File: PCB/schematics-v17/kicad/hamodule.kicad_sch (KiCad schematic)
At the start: 83 parts, among them J1 2604-1104, J10 EspSense, J11 Conn_01x02_Male, J12 NoCon, J2 2604-1102, J3 USB_C_Receptacle_USB2.0, J4 ESP Relays, J5 Current Jumper, J6 GND 3.3V, J7 Conn_01x02, J8 Current Jumper, J9 2604-1104, K1 PCN-105D, K2 PCN-105D, K3 PCN-105D, K4 PCN-105D, Q1 SS8050, Q2 SS8050, SW1 EN, SW2 IO0, U1 ULN2003A, U2 ESP32-WROOM-32E, U4 LD1117AV33_TO220, U5 MCP9700T-ETT, U6 LDA210-PDIP, U7 LDA210-PDIP, U8 CP2102N-A01-GQFN28

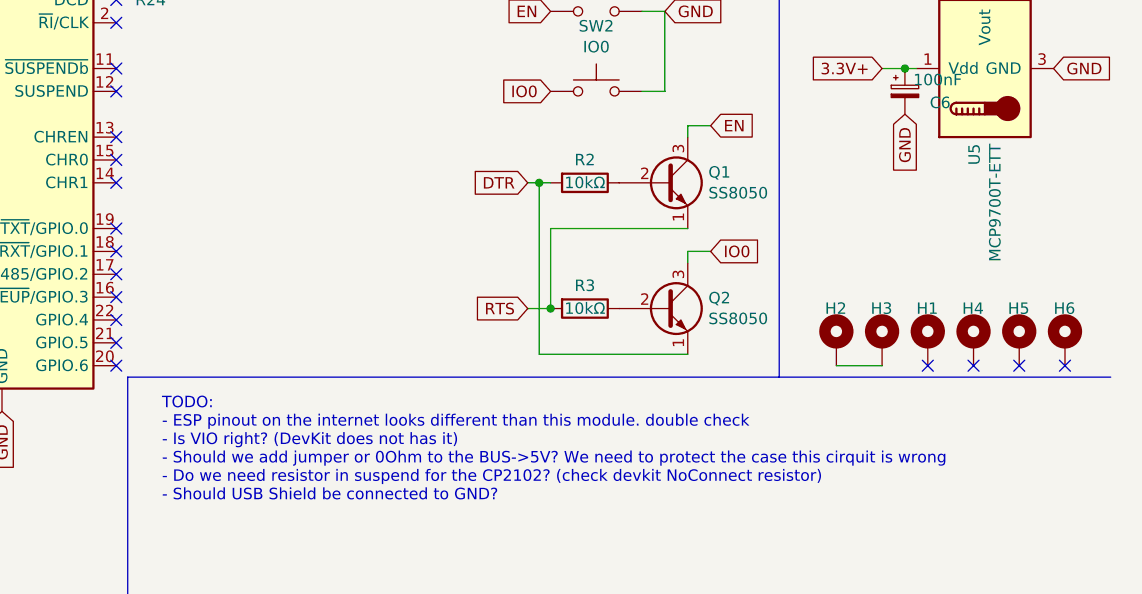
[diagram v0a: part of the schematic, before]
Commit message: fixing transistor symbol. pinout was wrong :(
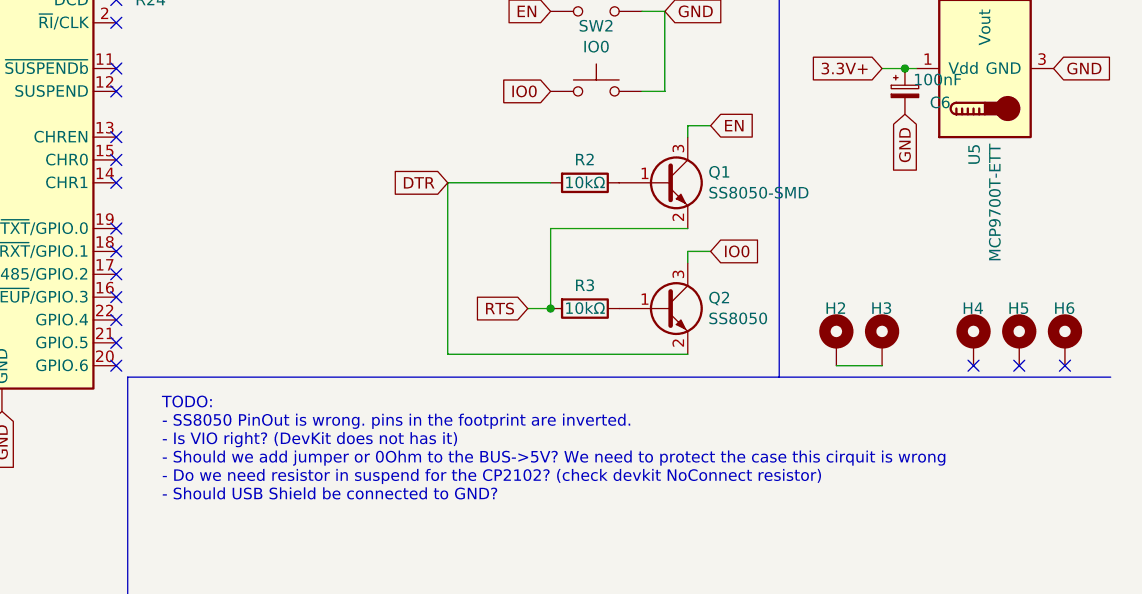
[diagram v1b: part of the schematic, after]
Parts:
- removed H1: MountingHole_Pad, MountingHole:MountingHole_3.2mm_M3_ISO14580_Pad, symbol Mechanical:MountingHole_Pad
- Q1: value SS8050 -> SS8050-SMD
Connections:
- net DTR: now also Q2.2 (E); no longer Q2.1 (E)
- net RTS: now also Q1.2 (E); no longer Q1.1 (E)
- net at R2.1: now also Q1.1 (B); no longer Q1.2 (B)
- net at R3.1: now also Q2.1 (B); no longer Q2.2 (B)
- no-connect marks 52 -> 51
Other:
- note added: "TODO: - SS8050 PinOut is wrong. pins in the footprint are inverted. - Is VIO right? (DevKit does not has it) - Should we add jumper or 0Ohm to the BUS->5V? We need to protect the case this cirquit is wrong - Do we need resistor in suspend for the CP2102? (check devkit NoConnect resistor) - Should USB Shield be connected to GND?"
- note removed: "TODO: - ESP pinout on the internet looks different than this module. double check - Is VIO right? (DevKit does not has it) - Should we add jumper or 0Ohm to the BUS->5V? We need to protect the case this cirquit is wrong - Do we need resistor in suspend for the CP2102? (check devkit NoConnect resistor) - Should USB Shield be connected to GND?"
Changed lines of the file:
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@@
   (junction (at 114.3 86.36) (diameter 0) (color 0 0 0 0)
   )
-  (junction (at 220.98 143.51) (diameter 0) (color 0 0 0 0)
-  )
   (junction (at 135.89 60.96) (diameter 0) (color 0 0 0 0)
   )
@@
   (no_connect (at 67.31 146.05))
   (no_connect (at 57.15 39.37))
-  (no_connect (at 264.16 163.83))
   (no_connect (at 173.99 148.59))
   (no_connect (at 173.99 161.29))
@@
     (stroke (width 0) (type default) (color 0 0 0 0))
   )
-  (wire (pts (xy 220.98 143.51) (xy 220.98 162.56))
-    (stroke (width 0) (type default) (color 0 0 0 0))
-  )
   (wire (pts (xy 106.68 86.36) (xy 114.3 86.36))
     (stroke (width 0) (type default) (color 0 0 0 0))
@@
     (stroke (width 0) (type default) (color 0 0 0 0))
   )
-  (wire (pts (xy 219.71 143.51) (xy 220.98 143.51))
+  (wire (pts (xy 210.82 143.51) (xy 222.25 143.51))
     (stroke (width 0) (type default) (color 0 0 0 0))
   )
@@
     (stroke (width 0) (type default) (color 0 0 0 0))
   )
+  (wire (pts (xy 210.82 162.56) (xy 237.49 162.56))
+    (stroke (width 0) (type default) (color 0 0 0 0))
+  )
   (wire (pts (xy 138.43 78.74) (xy 138.43 76.2))
     (stroke (width 0) (type default) (color 0 0 0 0))
@@
     (stroke (width 0) (type default) (color 0 0 0 0))
   )
-  (wire (pts (xy 220.98 162.56) (xy 237.49 162.56))
+  (wire (pts (xy 210.82 143.51) (xy 210.82 162.56))
     (stroke (width 0) (type default) (color 0 0 0 0))
   )
@@
     (stroke (width 0) (type default) (color 0 0 0 0))
   )
-  (wire (pts (xy 220.98 143.51) (xy 222.25 143.51))
-    (stroke (width 0) (type default) (color 0 0 0 0))
-  )
   (wire (pts (xy 97.79 157.48) (xy 99.06 157.48))
     (stroke (width 0) (type default) (color 0 0 0 0))
@@
     (stroke (width 0) (type default) (color 0 0 0 0))
   )
-  (text "TODO:\n- ESP pinout on the internet looks different than this module. double check\n- Is VIO right? (DevKit does not has it)\n- Should we add jumper or 0Ohm to the BUS->5V? We need to protect the case this cirquit is wrong\n- Do we need resistor in suspend for the CP2102? (check devkit NoConnect resistor)\n- Should USB Shield be connected to GND?"
+  (text "TODO:\n- SS8050 PinOut is wrong. pins in the footprint are inverted.\n- Is VIO right? (DevKit does not has it)\n- Should we add jumper or 0Ohm to the BUS->5V? We need to protect the case this cirquit is wrong\n- Do we need resistor in suspend for the CP2102? (check devkit NoConnect resistor)\n- Should USB Shield be connected to GND?"
     (at 179.07 179.07 0)
     (effects (font (size 1.27 1.27)) (justify left bottom))
@@
     )
   )
-  (global_label "DTR" (shape input) (at 219.71 143.51 180) (fields_autoplaced)
+  (global_label "DTR" (shape input) (at 210.82 143.51 180) (fields_autoplaced)
     (effects (font (size 1.27 1.27)) (justify right))
-    (property "Intersheet References" "${INTERSHEET_REFS}" (id 0) (at 40.64 0 0)
+    (property "Intersheet References" "${INTERSHEET_REFS}" (id 0) (at 31.75 0 0)
       (effects (font (size 1.27 1.27)) hide)
     )
@@
     (pin "2")
   )
-  (symbol (lib_id "Mechanical:MountingHole_Pad") (at 264.16 161.29 0) (unit 1)
-    (in_bom yes) (on_board yes)
-    (property "Reference" "H1" (id 0) (at 262.89 157.48 0)
-      (effects (font (size 1.27 1.27)) (justify left))
-    )
-    (property "Value" "MountingHole_Pad" (id 1) (at 266.7 162.3568 0)
-      (effects (font (size 1.27 1.27)) (justify left) hide)
-    )
-    (property "Footprint" "MountingHole:MountingHole_3.2mm_M3_ISO14580_Pad" (id 2) (at 264.16 161.29 0)
-      (effects (font (size 1.27 1.27)) hide)
-    )
-    (property "Datasheet" "~" (id 3) (at 264.16 161.29 0)
-      (effects (font (size 1.27 1.27)) hide)
-    )
-    (pin "1")
-  )
   (symbol (lib_id "wago-2604-1104:2604-1104") (at 215.9 31.75 180) (unit 1)
     (in_bom yes) (on_board yes)
@@
     (pin "2")
   )
-  (symbol (lib_id "Transistor_BJT:2N2219") (at 234.95 143.51 0) (unit 1)
+  (symbol (lib_name "2N2219_1") (lib_id "Transistor_BJT:2N2219") (at 234.95 143.51 0) (unit 1)
     (in_bom yes) (on_board yes)
     (property "Reference" "Q1" (id 0) (at 239.776 142.3416 0)
       (effects (font (size 1.27 1.27)) (justify left))
     )
-    (property "Value" "SS8050" (id 1) (at 239.776 144.653 0)
+    (property "Value" "SS8050-SMD" (id 1) (at 239.776 144.653 0)
       (effects (font (size 1.27 1.27)) (justify left))
     )
@@
       (effects (font (size 1.27 1.27)) hide)
     )
-    (pin "1")
     (pin "2")
+    (pin "1")
     (pin "3")
   )
@@
     (pin "2")
   )
-  (symbol (lib_id "Transistor_BJT:2N2219") (at 234.95 157.48 0) (unit 1)
-    (in_bom yes) (on_board yes)
-    (property "Reference" "Q2" (id 0) (at 239.776 156.3116 0)
-      (effects (font (size 1.27 1.27)) (justify left))
-    )
-    (property "Value" "SS8050" (id 1) (at 239.776 158.623 0)
-      (effects (font (size 1.27 1.27)) (justify left))
-    )
-    (property "Footprint" "Package_TO_SOT_SMD:SOT-23" (id 2) (at 240.03 159.385 0)
-      (effects (font (size 1.27 1.27) italic) (justify left) hide)
-    )
-    (property "Datasheet" "http://www.onsemi.com/pub_link/Collateral/2N2219-D.PDF" (id 3) (at 234.95 157.48 0)
-      (effects (font (size 1.27 1.27)) (justify left) hide)
-    )
-    (property "JLCPCB" "C177739" (id 4) (at 234.95 157.48 0)
-      (effects (font (size 1.27 1.27)) hide)
-    )
-    (pin "1")
-    (pin "2")
-    (pin "3")
-  )
   (symbol (lib_id "Device:R") (at 27.94 120.65 180) (unit 1)
     (in_bom yes) (on_board yes)
@@
     (pin "S1")
   )
+  (symbol (lib_name "2N2219_1") (lib_id "Transistor_BJT:2N2219") (at 234.95 157.48 0) (unit 1)
+    (in_bom yes) (on_board yes)
+    (property "Reference" "Q2" (id 0) (at 239.776 156.3116 0)
+      (effects (font (size 1.27 1.27)) (justify left))
+    )
+    (property "Value" "SS8050" (id 1) (at 239.776 158.623 0)
+      (effects (font (size 1.27 1.27)) (justify left))
+    )
+    (property "Footprint" "Package_TO_SOT_SMD:SOT-23" (id 2) (at 240.03 159.385 0)
+      (effects (font (size 1.27 1.27) italic) (justify left) hide)
+    )
+    (property "Datasheet" "http://www.onsemi.com/pub_link/Collateral/2N2219-D.PDF" (id 3) (at 234.95 157.48 0)
+      (effects (font (size 1.27 1.27)) (justify left) hide)
+    )
+    (property "JLCPCB" "C177739" (id 4) (at 234.95 157.48 0)
+      (effects (font (size 1.27 1.27)) hide)
+    )
+    (pin "1")
+    (pin "2")
+    (pin "3")
+  )
   (sheet_instances
     (path "/" (page "1"))
@@
       (reference "F2") (unit 1) (value "250v50mA") (footprint "Fuse:Fuse_Littelfuse_372_D8.50mm")
     )
-    (path "/00000000-0000-0000-0000-0000618c5da5"
-      (reference "H1") (unit 1) (value "MountingHole_Pad") (footprint "MountingHole:MountingHole_3.2mm_M3_ISO14580_Pad")
-    )
     (path "/00000000-0000-0000-0000-000061d119d5"
       (reference "H2") (unit 1) (value "MountingHole_Pad") (footprint "MountingHole:MountingHole_2.2mm_M2_DIN965_Pad_TopOnly")
@@
     )
     (path "/00000000-0000-0000-0000-000061ae6901"
-      (reference "Q1") (unit 1) (value "SS8050") (footprint "Package_TO_SOT_SMD:SOT-23")
+      (reference "Q1") (unit 1) (value "SS8050-SMD") (footprint "Package_TO_SOT_SMD:SOT-23")
     )
-    (path "/00000000-0000-0000-0000-000061ae691e"
+    (path "/d663e8db-4355-4b8a-9c66-87d3ccecefc9"
       (reference "Q2") (unit 1) (value "SS8050") (footprint "Package_TO_SOT_SMD:SOT-23")
     )

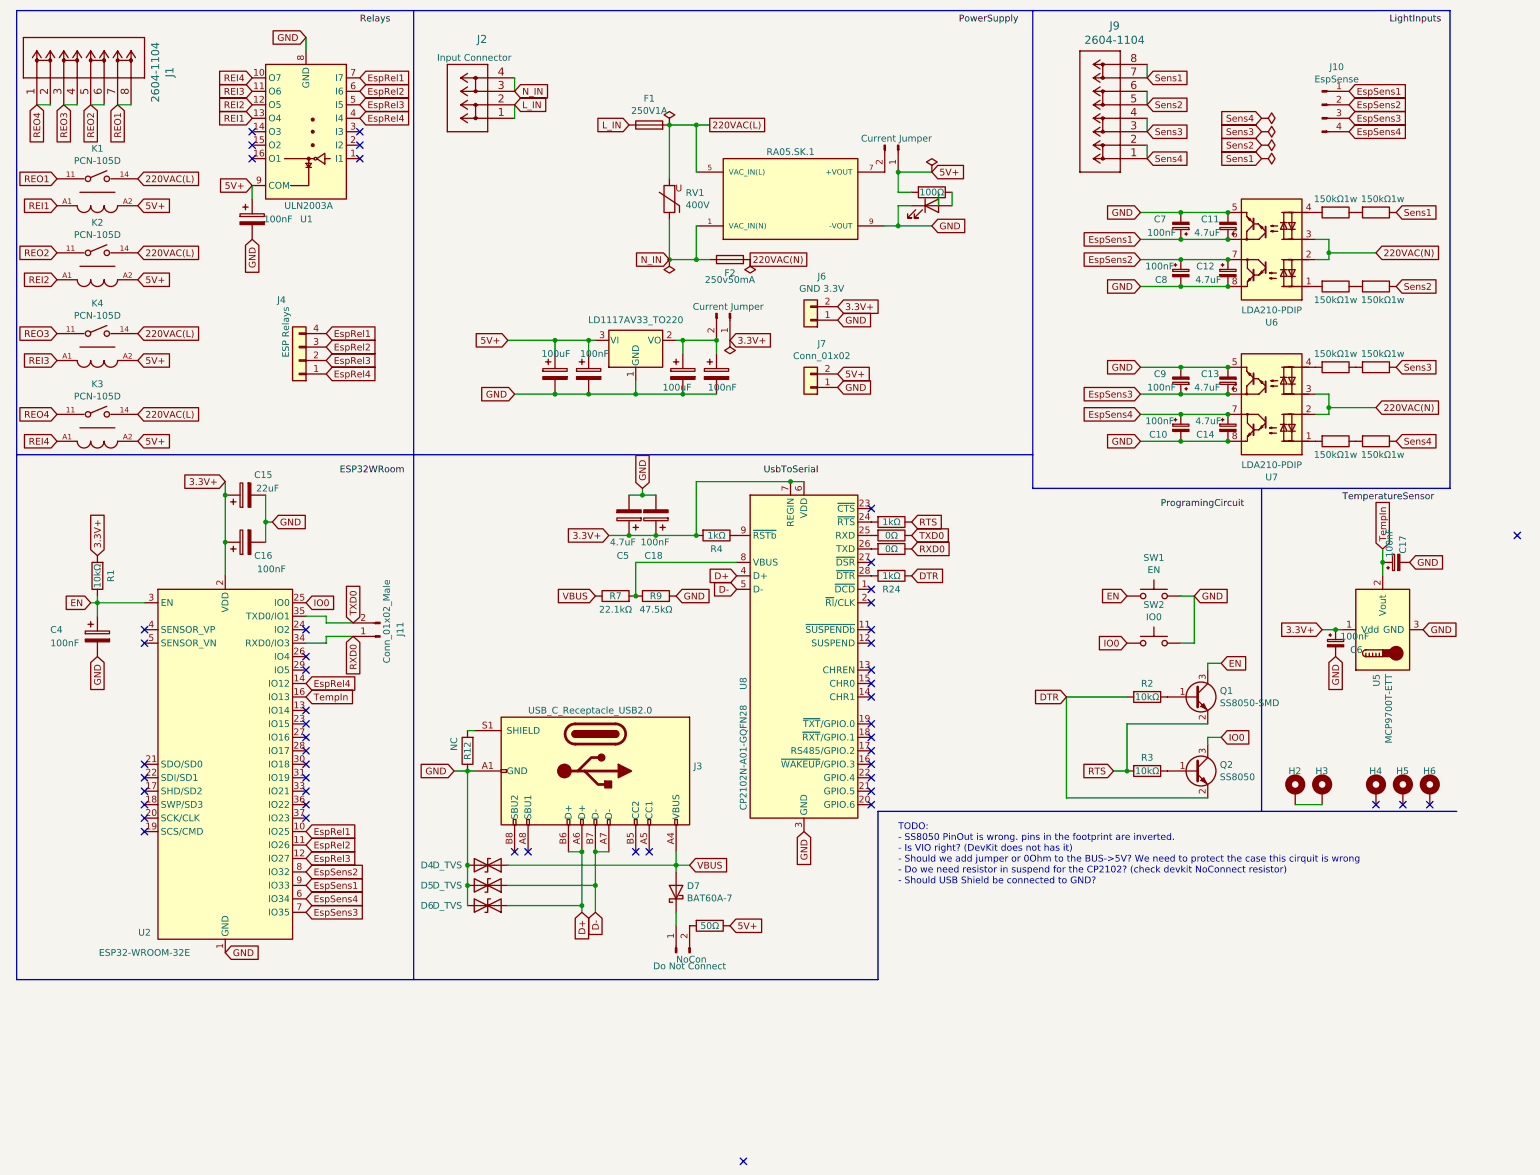
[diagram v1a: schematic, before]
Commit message: fixing kicad6 library reference. Using the right transistor package. Fixing 3D for some components
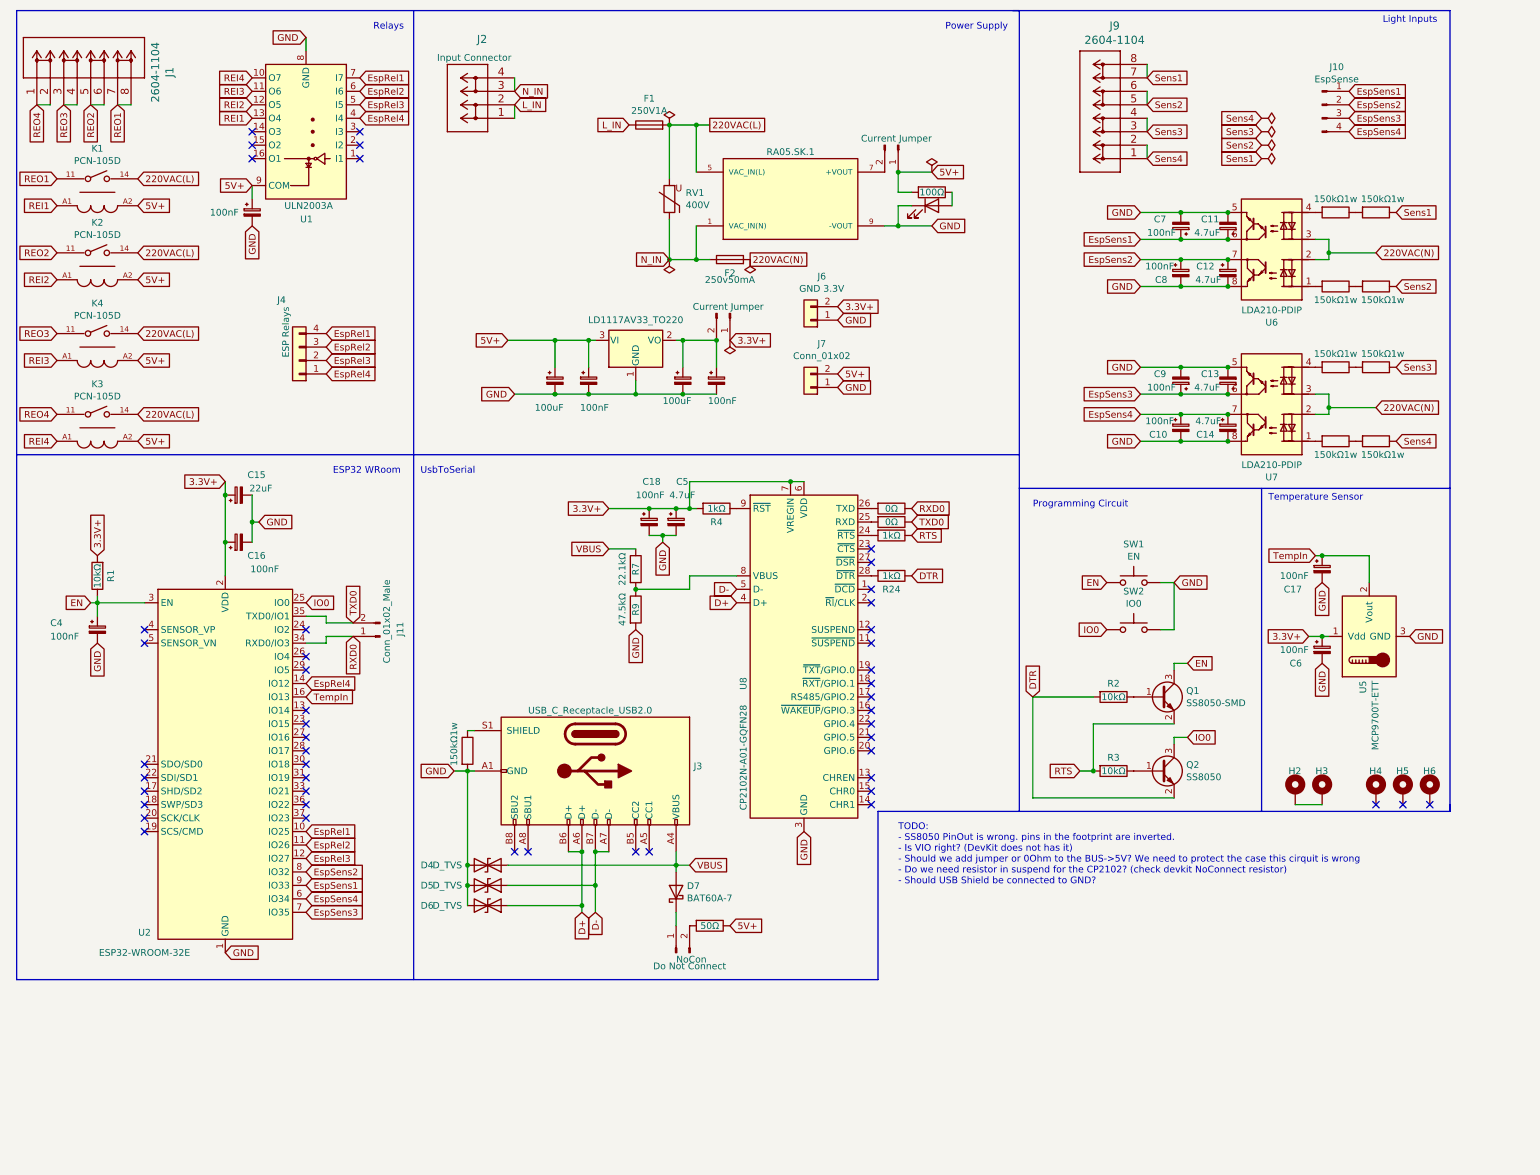
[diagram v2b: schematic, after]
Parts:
- 100uF_1, 100uF_2, C1, C15, C16, C18, C2, C3, C4, C5: symbol Device:CP -> Device:C_Polarized_Small
- C10, C17, C6, C7, C8, C9: symbol Device:CP_Small -> Device:C_Polarized_Small
- C11, C12, C13, C14: footprint Capacitor_SMD:C_1206_3216Metric_Pad1.42x1.75mm_HandSolder -> Capacitor_SMD:C_1206_3216Metric_Pad1.33x1.80mm_HandSolder; symbol Device:CP_Small -> Device:C_Polarized_Small
- Q1, Q2: symbol Transistor_BJT:2N2219 -> Device:Q_NPN_BEC
- R10: JLCPCB (none) -> C17738
- R12: value NC -> 150kΩ1w; footprint Resistor_SMD:R_0603_1608Metric_Pad0.98x0.95mm_HandSolder -> Resistor_SMD:R_2512_6332Metric_Pad1.40x3.35mm_HandSolder; JLCPCB (none) -> C25719
- R16, R17, R18, R19, R20, R21, R22, R23: footprint Resistor_SMD:R_2512_6332Metric_Pad1.52x3.35mm_HandSolder -> Resistor_SMD:R_2512_6332Metric_Pad1.40x3.35mm_HandSolder
- RA05.SK.1: symbol RAC05-05SK_277:RAC05-05SK_277 -> RAC05-05SK_277:RAC05-05SK/277
- U8: symbol Interface_USB:CP2102N-A01-GQFN28 -> Interface_USB:CP2102N-Axx-xQFN28
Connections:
- net GND: now also R12.2; no longer R12.1
- net at J3.S1 (SHIELD): now also R12.1; no longer R12.2
- no-connect marks 51 -> 49
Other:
- note added: "ESP32 WRoom"
- note added: "Light Inputs"
- note added: "Power Supply"
- note added: "Programming Circuit"
- note added: "Relays"
- note added: "Temperature Sensor"
- note added: "UsbToSerial"
- moved on the sheet: C15, C16, C17, C18, C4, C5, C6, Q1, Q2, R2, R3, R4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
